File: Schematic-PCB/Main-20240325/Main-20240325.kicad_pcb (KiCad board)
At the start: 2 copper layers, 115 x 115 mm, 104 parts, among them J1 Conn_01x10_Pin, J2 Conn_01x03_Pin, J3 Conn_01x15_Pin, J4 Conn_02x05_Odd_Even, J5 Conn_01x04_Pin, U1 DEV-16771, U10 TSSP58038, U11 TSSP58038, U12 TSSP58038, U13 TSSP58038, U14 TSSP58038, U15 TSSP58038, U16 TSSP58038, U17 TSSP58038, U18 TSSP58038, U19 TSSP58038, U4 TSSP58038, U5 TSSP58038, U6 TSSP58038, U7 TSSP58038, U8 TSSP58038, U9 TSSP58038

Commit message: メイン基板仮完成
DRおねがい
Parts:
- moved C7 0.09 mm to (-39.9, -14.8)
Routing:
- net Cam_SS: track 82.8 -> 36.8 mm
- net MOSI: track 72.3 -> 31.7 mm
- net SW-TAC-2: track 77.1 -> 37.7 mm, vias 1 -> 0
- net SW-TAC-1: track 79.8 -> 41.9 mm, vias 1 -> 0
- net MISO: track 68.5 -> 30.8 mm
- net BUZZER: track 98.9 -> 66.5 mm, vias 2 -> 1
- net Cam-RX: track 52.7 -> 30.5 mm
- net SW-TAC-3: track 73.4 -> 56.0 mm
- net SW-TAC-4: track 73.9 -> 56.7 mm
- net Cam-TX: track 52.3 -> 39.0 mm
- net KickerSignal: track 141.4 -> 129.7 mm
- net GND: vias 16 -> 17

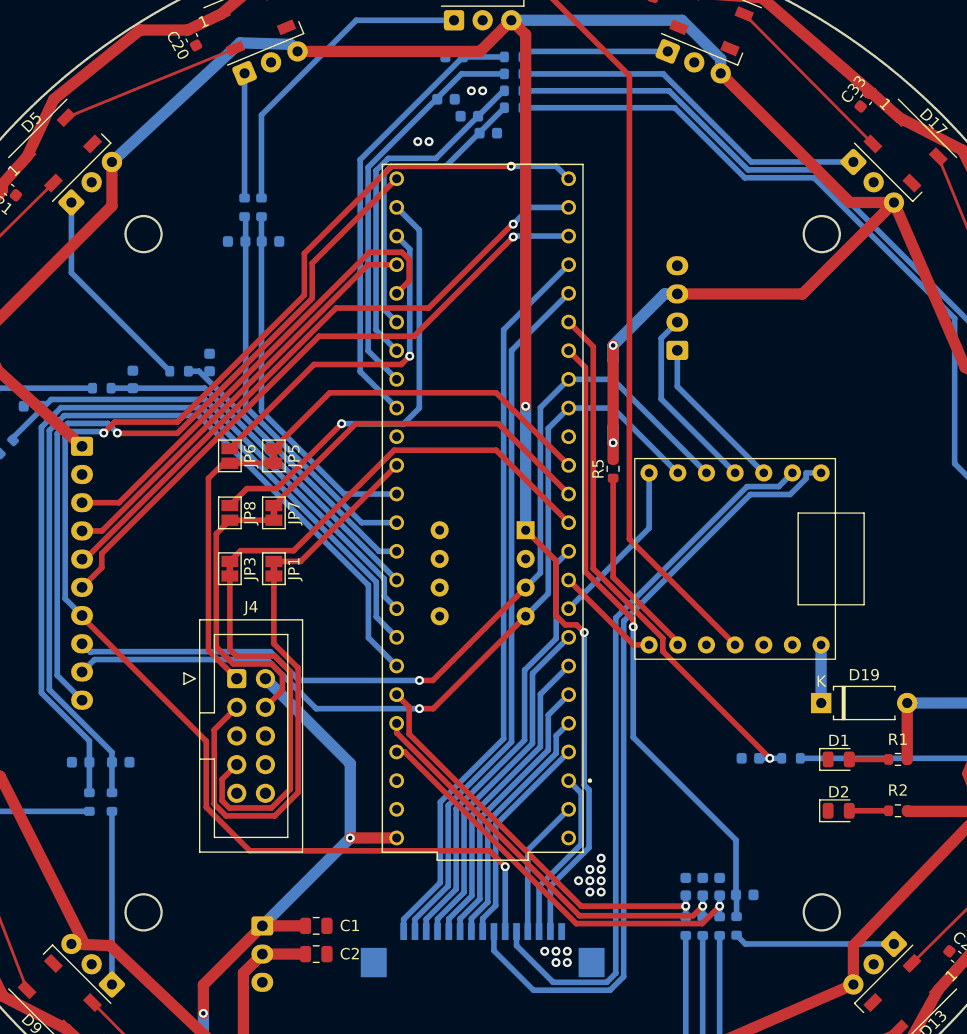
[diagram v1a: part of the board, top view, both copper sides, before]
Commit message: ラインセンサ基板とメイン基板のDR進めたよ
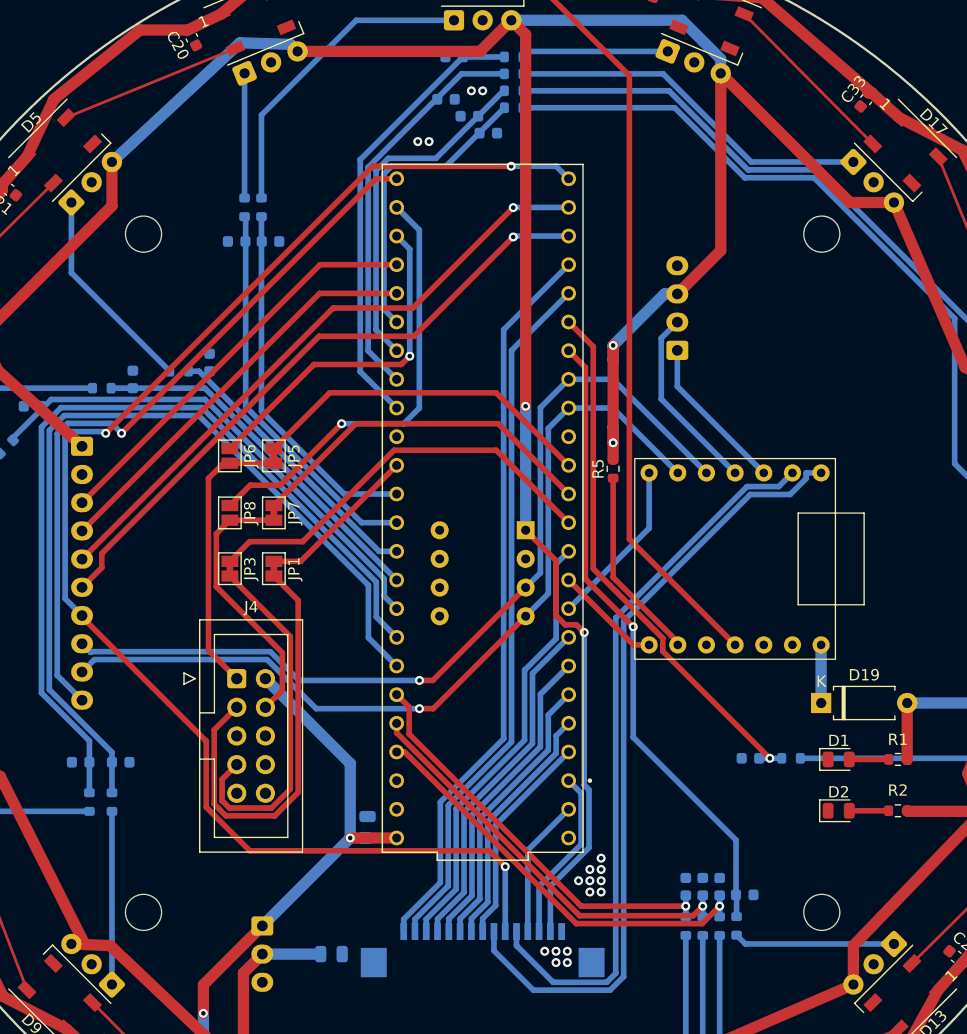
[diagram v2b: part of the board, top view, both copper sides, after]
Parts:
- added REF**: MountingHole_3.2mm_M3, MountingHole:MountingHole_3.2mm_M3, F.Cu at (-30.1, -30.1)
- added REF**: MountingHole_3.2mm_M3, MountingHole:MountingHole_3.2mm_M3, F.Cu at (30.1, 30.1)
- added REF**: MountingHole_3.2mm_M3, MountingHole:MountingHole_3.2mm_M3, F.Cu at (-30.1, 30.1)
- added REF**: MountingHole_3.2mm_M3, MountingHole:MountingHole_3.2mm_M3, F.Cu at (30.1, -30.1)
- C1, C2: moved to B.Cu
- moved C1 9.85 mm to (-10.2, 22.5), turned to 90 degrees
- moved C2 1.35 mm to (-13.4, 33.8)
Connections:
- U1 pad 36: SW-TAC-2 -> SW-TAC-1
- U1 pad 37: SW-TAC-1 -> SW-TAC-2
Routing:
- net SW-TAC-1: track 41.9 -> 36.6 mm
- net +5V: track 437.4 -> 435.1 mm
- net KickerSignal: track 129.7 -> 127.6 mm
- net Net-(J4-Pin_7): track 33.8 -> 31.8 mm
- net Cam-MOSI_TX: track 26.0 -> 24.0 mm
- net BUZZER: track 66.5 -> 64.7 mm
- net SW-TAC-2: track 37.7 -> 36.6 mm
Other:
- outline, holes or cut-outs redrawn

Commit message: メイン基板のDRを進めたよ
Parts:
- moved C15 62.3 mm to (46.0, 3.50), turned to -90 degrees
- moved R18 57.4 mm to (46.0, -3.50), turned to -90 degrees
- moved C16 52.1 mm to (43.8, -14.4), turned to -67.5 degrees
- moved R19 44.2 mm to (41.2, -20.8), turned to -67.5 degrees
- moved C10 41.1 mm to (-20.8, 41.2), turned to 157.5 degrees
- moved C17 40.1 mm to (35.0, -30.1), turned to -45 degrees
- moved R13 34.7 mm to (-14.4, 43.8), turned to 157.5 degrees
- moved C11 29.3 mm to (-3.50, 46.0), turned to 180 degrees
- moved R20 28.8 mm to (30.1, -35.0), turned to -45 degrees
- moved C3 27.8 mm to (3.50, -46.0)
- moved C18 23.8 mm to (20.8, -41.2), turned to -22.5 degrees
- moved R14 21.7 mm to (3.50, 46.0), turned to 180 degrees
- moved R6 21.1 mm to (-3.50, -46.0), turned to 0 degrees
- moved C14 18.0 mm to (41.2, 20.8), turned to -112.5 degrees
- moved C12 17.4 mm to (14.4, 43.8), turned to -157.5 degrees
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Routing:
- net Net-(U16-OUT): track 69.0 -> 3.49 mm
- net ball13: track 26.7 -> 86.5 mm, vias 0 -> 1
- net ball14: track 31.1 -> 80.5 mm, vias 0 -> 1
- net Net-(U17-OUT): track 49.7 -> 3.49 mm
- net Net-(U11-OUT): track 47.0 -> 3.49 mm
- net ball08: track 36.7 -> 77.3 mm
- net ball07: track 77.6 -> 44.6 mm, vias 0 -> 1
- net Net-(U18-OUT): track 32.5 -> 3.49 mm
- net ball15: track 35.3 -> 63.9 mm, vias 0 -> 1
- net Net-(U12-OUT): track 29.3 -> 3.49 mm
- net Net-(U4-OUT): track 27.9 -> 3.49 mm
- net ball12: track 48.0 -> 71.6 mm
- net ball06: track 76.6 -> 53.6 mm, vias 0 -> 1
- net ball03: track 25.0 -> 47.4 mm
- net ball09: track 36.9 -> 59.3 mm
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
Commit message: メイン基板のDR完了
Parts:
- J3: footprint @2024-MD:1.0K-FX-15PWB -> @2024TOINIOT2-MD:1.0K-FX-15PWB
- R1, R2: moved to B.Cu
- moved C2 1.34 mm to (-14.3, 32.8), turned to 90 degrees
- renumbered D2 to 3.3V, D1 to 5V, JP5 to MISO, JP7 to MOSI, JP6 to RX, JP1 to SCK, JP3 to SS, JP8 to TX
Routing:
- net +3.3V: track 483.3 -> 479.6 mm, vias 4 -> 5
- net +5V: track 434.2 -> 431.6 mm
- net ball01k: track 73.5 -> 72.2 mm
- net ball02k: track 69.0 -> 67.7 mm
- net KickerSignal: track 125.1 -> 123.7 mm
- net EN-1: track 65.1 -> 63.8 mm
- net PH-1: track 62.2 -> 60.9 mm
- net ball14: track 80.5 -> 79.4 mm
- net ball13: track 86.5 -> 85.4 mm
- net EN-2: track 38.9 -> 37.9 mm
- net ball15: track 63.9 -> 62.9 mm
- net ball12: track 71.6 -> 70.7 mm
- net ball07: track 44.6 -> 43.7 mm
- net ball08: track 77.3 -> 76.4 mm
- net SCL: track 77.0 -> 76.2 mm
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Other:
- board text added: "3.3V"
- board text added: "5V"
- board text added: "GND"

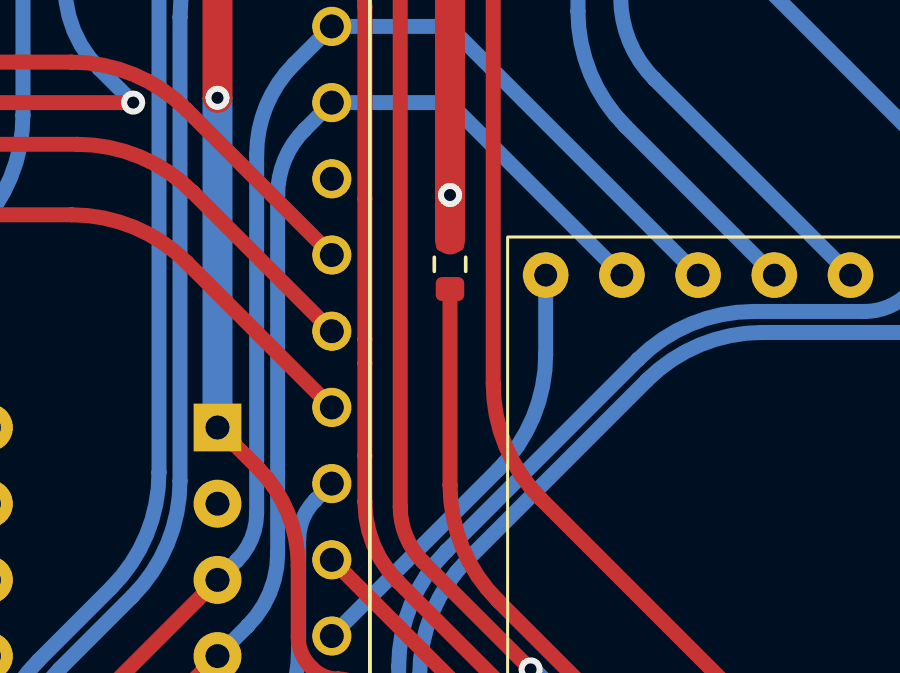
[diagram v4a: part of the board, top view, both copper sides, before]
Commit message: キッカー基板を更新した
MDとの接続をピンヘッダ/ピンソケットを使う方式に変更した
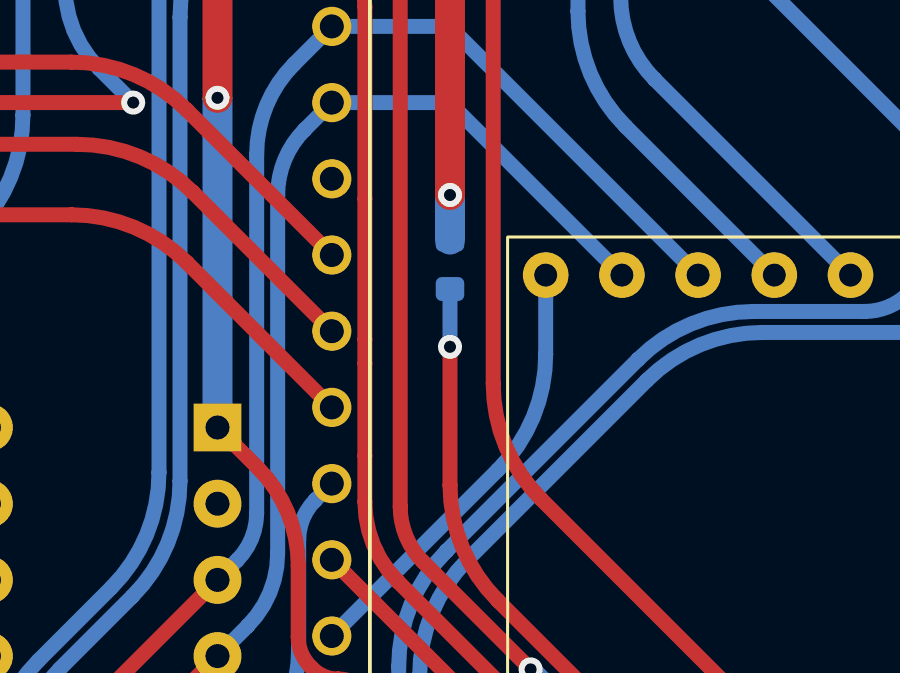
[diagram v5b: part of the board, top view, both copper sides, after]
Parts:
- R5: moved to B.Cu
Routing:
- net Net-(U2-SCK_D8): vias 0 -> 1

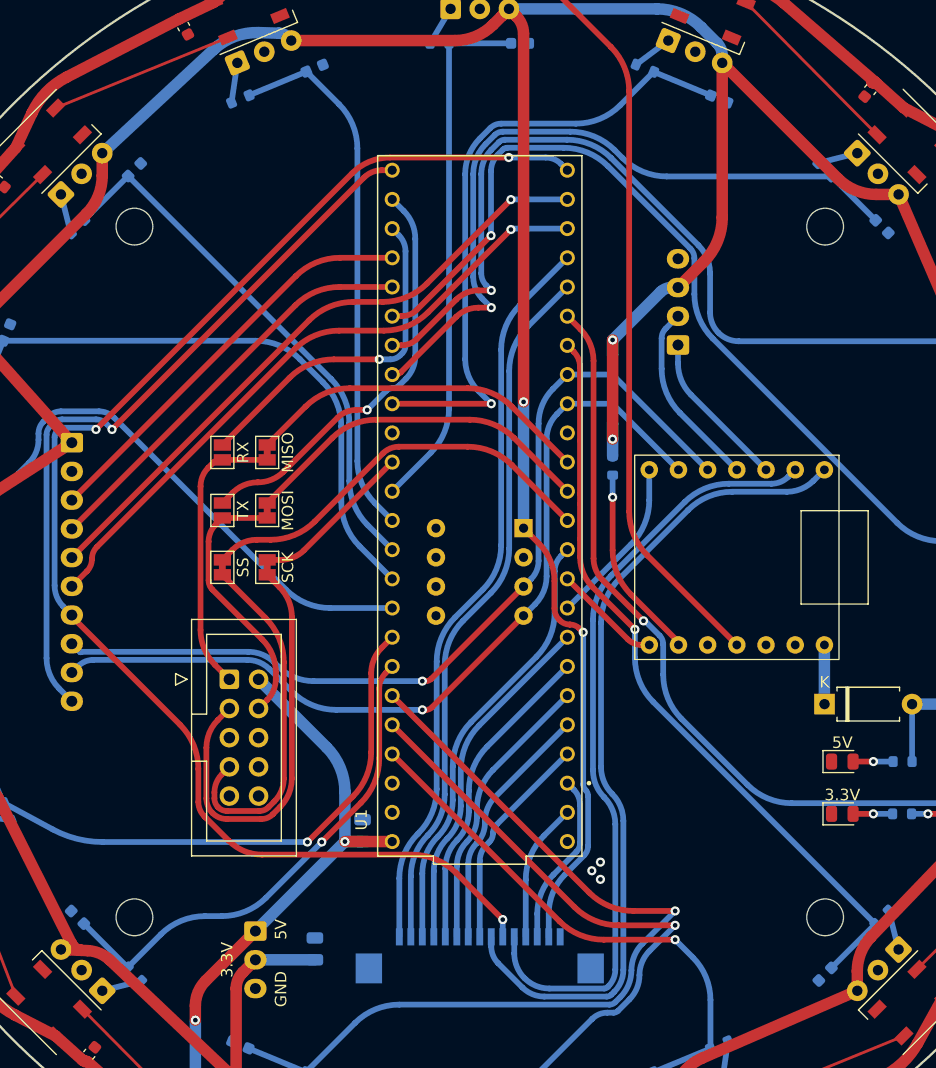
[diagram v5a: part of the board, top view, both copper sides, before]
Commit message: FPC/FCCコネクタの順番を変更した
斜めに挿入・逆向きに挿入したときに+3.3VとGNDがショートしないようにした
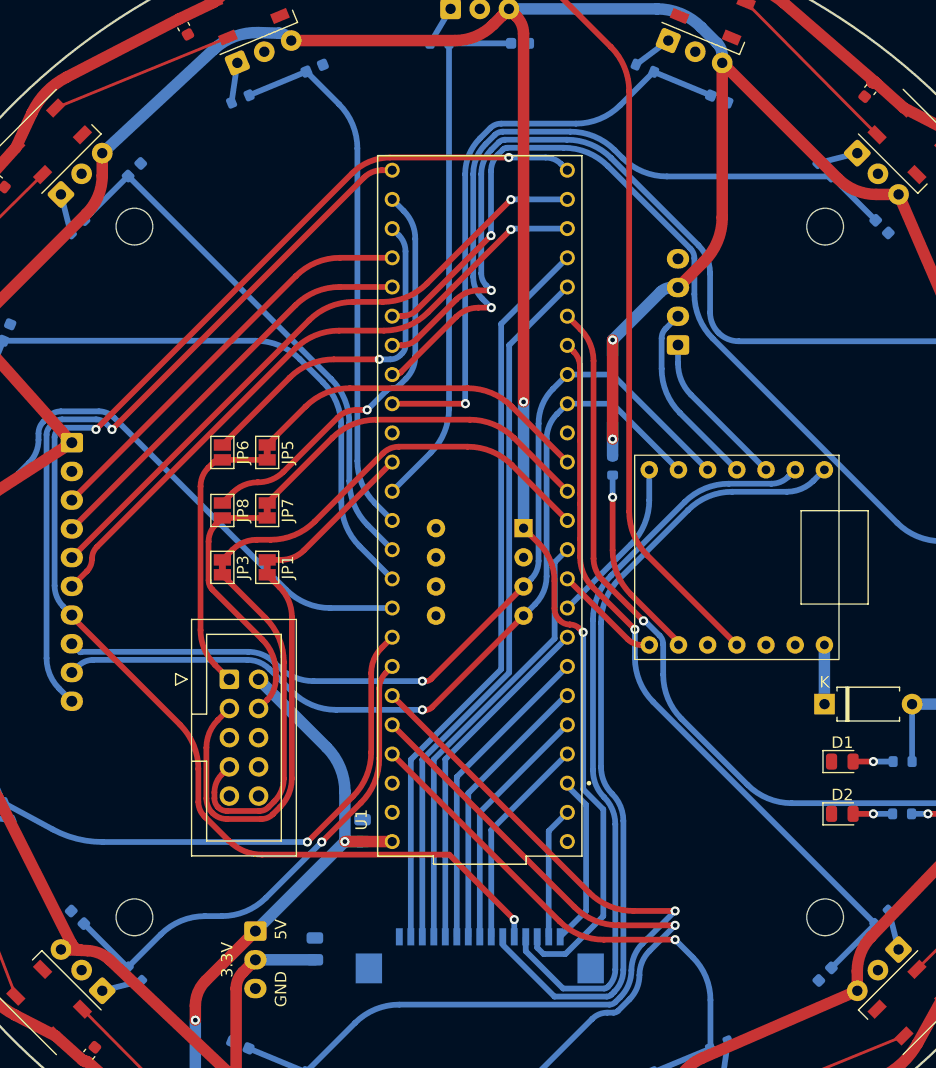
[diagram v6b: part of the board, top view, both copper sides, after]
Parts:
- renumbered 5V to D1, 3.3V to D2, SCK to JP1, SS to JP3, MISO to JP5, RX to JP6, MOSI to JP7, TX to JP8
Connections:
- J3 pad 1: GND -> Line-RX
- J3 pad 10: PH-3 -> EN-3
- J3 pad 11: EN-3 -> PH-2
- J3 pad 12: PH-2 -> EN-2
- J3 pad 13: EN-2 -> PH-1
- J3 pad 14: PH-1 -> EN-1
- J3 pad 15: EN-1 -> GND
- J3 pad 2: +3.3V -> Line-TX
- J3 pad 3: Line-RX -> +3.3V
- J3 pad 4: Line-TX -> ball02k
- J3 pad 5: ball02k -> KickerSignal
- J3 pad 6: KickerSignal -> ball01k
- J3 pad 7: ball01k -> PH-4
- J3 pad 8: PH-4 -> EN-4
- J3 pad 9: EN-4 -> PH-3
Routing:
- net +3.3V: track 479.6 -> 485.6 mm
- net ball16: track 55.4 -> 52.4 mm
- net ball01k: track 72.2 -> 70.1 mm
- net ball02k: track 67.7 -> 66.1 mm
- net KickerSignal: track 123.7 -> 125.0 mm
- net EN-1: track 63.8 -> 64.7 mm
- net PH-1: track 60.9 -> 61.8 mm
- net EN-2: track 37.9 -> 38.5 mm
- net Line-TX: track 12.1 -> 11.5 mm
- net GND: vias 3 -> 0

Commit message: メイン基板とかいろいろ編集した
ネオピの位置どうしよう...
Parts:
- added D3: WS2812B, LED_SMD:LED_WS2812B_PLCC4_5.0x5.0mm_P3.2mm, F.Cu at (-29.5, -77.0)
- added U4: TSSP58038, @2024TOINIOT2-Main:Vishay_MINICAST-3Pin, B.Cu at (-29.5, -77.0)

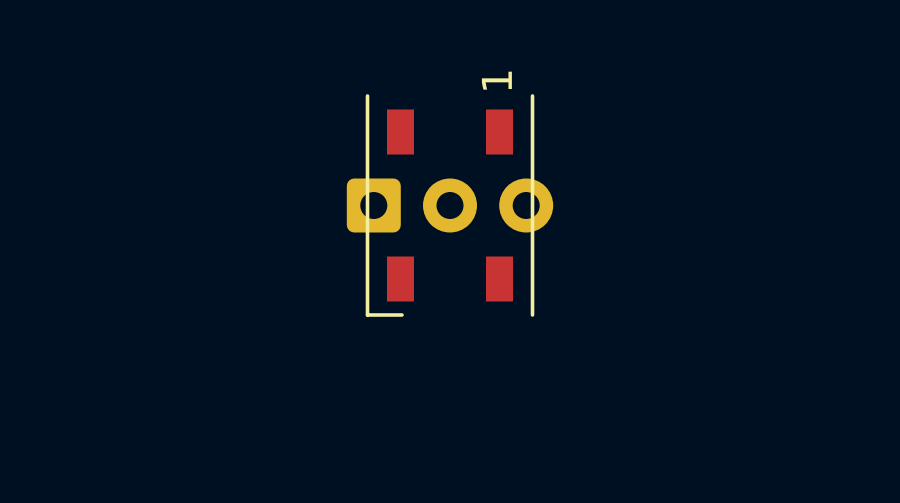
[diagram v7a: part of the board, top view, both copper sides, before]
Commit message: 旧機体用の守りプログラムを編集+メイン基板の回路図を編集
メイン基板に電源用スイッチを追加したりしてみた
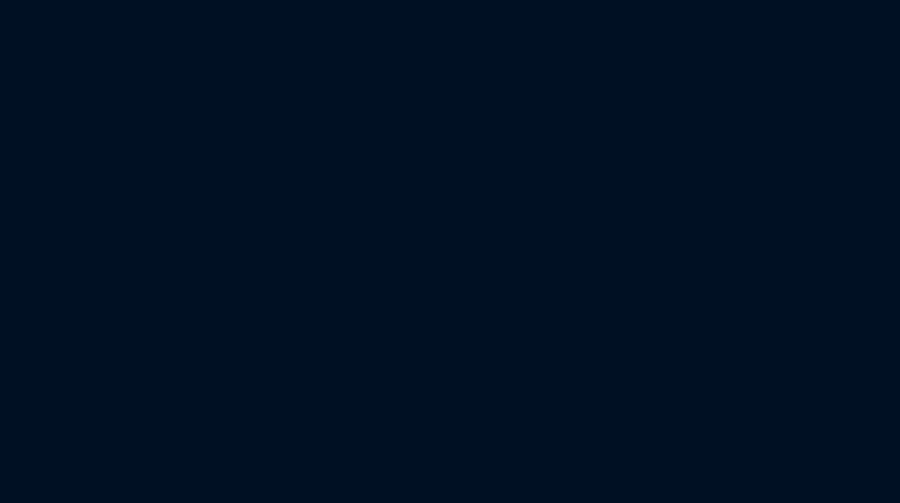
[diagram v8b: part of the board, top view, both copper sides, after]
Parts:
- removed the D3 at (-29.5, -77.0)
- removed the U4 at (-29.5, -77.0)
